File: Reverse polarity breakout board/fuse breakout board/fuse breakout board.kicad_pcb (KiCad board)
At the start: 2 copper layers, 8 parts

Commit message: yeo
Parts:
- moved Conn2 2.55 mm to (49.4, 44.1)
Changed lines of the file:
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@@
 	(footprint "MRDT_Connectors:Anderson_1_Horizontal"
 		(layer "F.Cu")
-		(at 49.8518 41.627)
+		(at 49.3518 44.127)
 		(property "Reference" "Conn2"
 			(at -5.588 4.572 0)

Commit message: We are almost finished
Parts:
- moved Conn2 83.3 mm to (61.1, 126.6)
- moved D1 81.0 mm to (85.3, 110.5)
- moved Conn1 56.5 mm to (61.1, 85.0)
- moved C4 47.9 mm to (97.6, 77.2)
- moved F1 47.7 mm to (87.4, 92.7), turned to -90 degrees
- moved C3 43.0 mm to (72.1, 68.5), turned to 90 degrees
- moved C1 37.9 mm to (89.9, 68.1), turned to 90 degrees
- moved C2 31.9 mm to (59.4, 70.6), turned to 180 degrees
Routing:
- added copper zone on F.Cu, net +BATT
- added copper zone on B.Cu, net GND
- added copper zone on F.Cu, net Net-(D1-K)
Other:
- board outline added: 69.6 x 82.8 mm
- board text added: "Reverse Polarity Fuse Board, Rev 1 Mars Rover Design Team Missouri S&T, 2024 Luke Duff, Sean Duda, Ethan Coggschell"

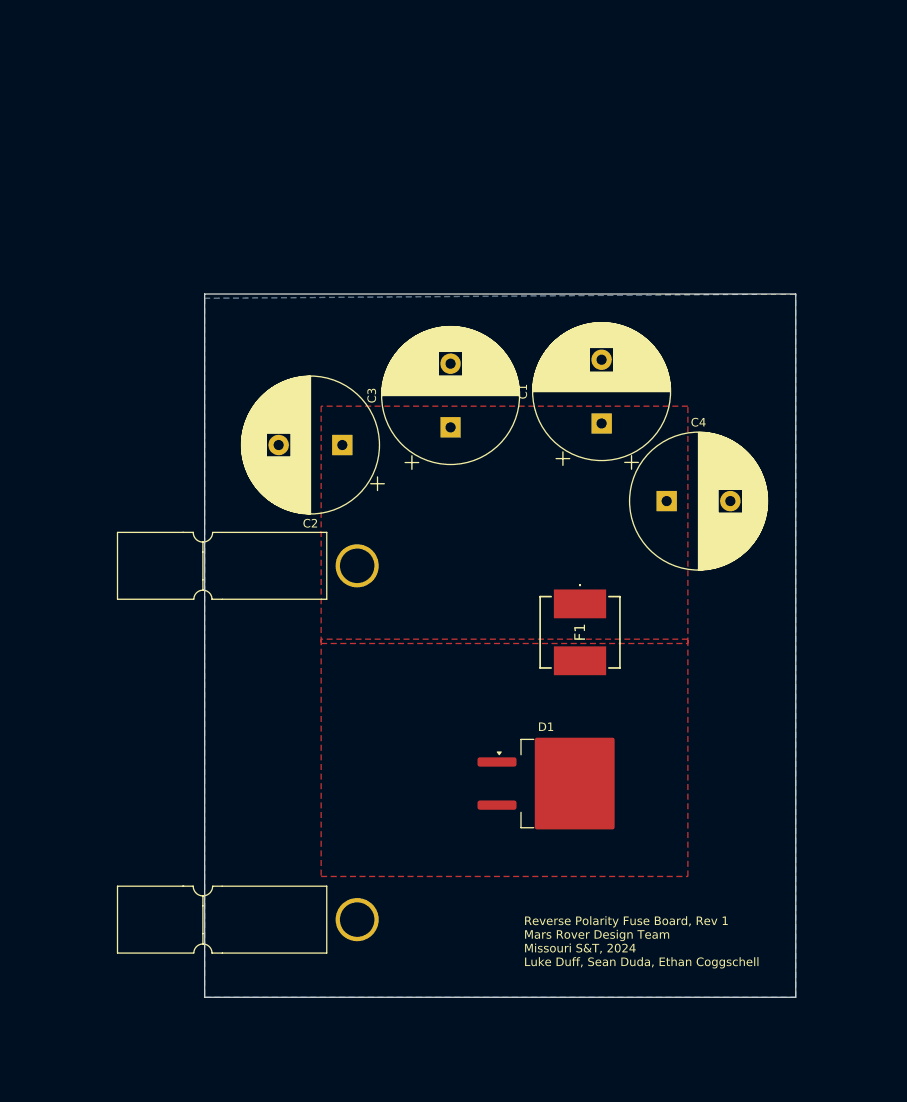
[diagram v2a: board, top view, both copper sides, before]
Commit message: Reworked power planes and adjusted cap bank
Reworked power plane and adjusted cap bank. Created a 35 mill trace from heatsink die to pad off power plane to account for ground connection
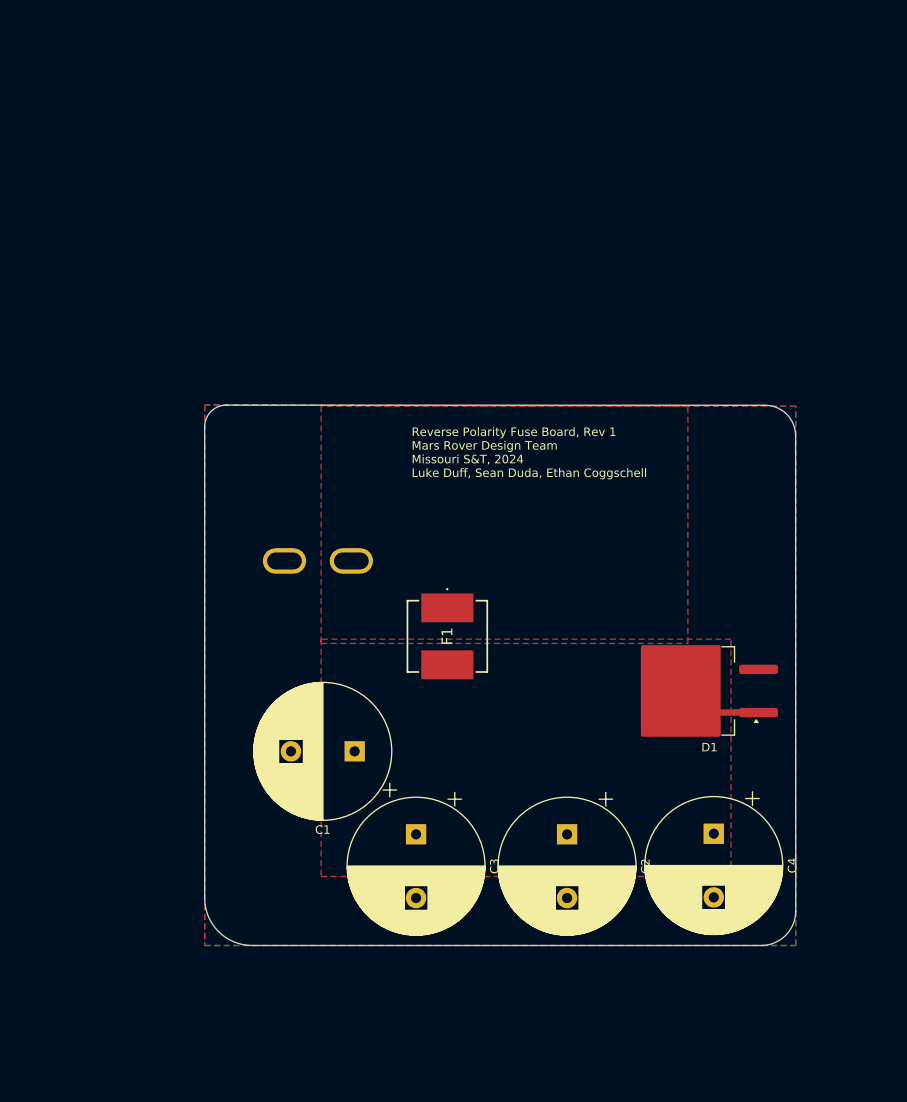
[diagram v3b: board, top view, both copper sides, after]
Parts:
- removed Conn2: AndersonPP, MRDT_Connectors:Anderson_1_Horizontal
- Conn1: footprint MRDT_Connectors:Anderson_1_Horizontal -> MRDT_Connectors:Square_Anderson_2_H_Side_By_Side_PV; moved to B.Cu
- moved C2 52.9 mm to (85.9, 116.5), turned to -90 degrees
- moved C1 48.3 mm to (60.8, 106.7), turned to 180 degrees
- moved C3 48.1 mm to (68.1, 116.5), turned to -90 degrees
- moved C4 39.5 mm to (103.1, 116.4), turned to -90 degrees
- moved D1 18.9 mm to (100.7, 99.6), turned to 180 degrees
- moved F1 15.6 mm to (71.8, 93.1)
- moved Conn1 8.85 mm to (52.3, 84.4), turned to -90 degrees
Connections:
- Conn1 pad 1: (no net) -> GND
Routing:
- net Net-(D1-K): track 0.00 -> 10.2 mm
- added copper zone on F.Cu, net GND
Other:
- board size 69.6 x 82.8 mm -> 69.6 x 63.6 mm

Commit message: Added Load Tester andersons and via stitching
Added load tester andersons and vias to stitch ground planes on the front and back together to prevent capacitance build up and allow current to flow
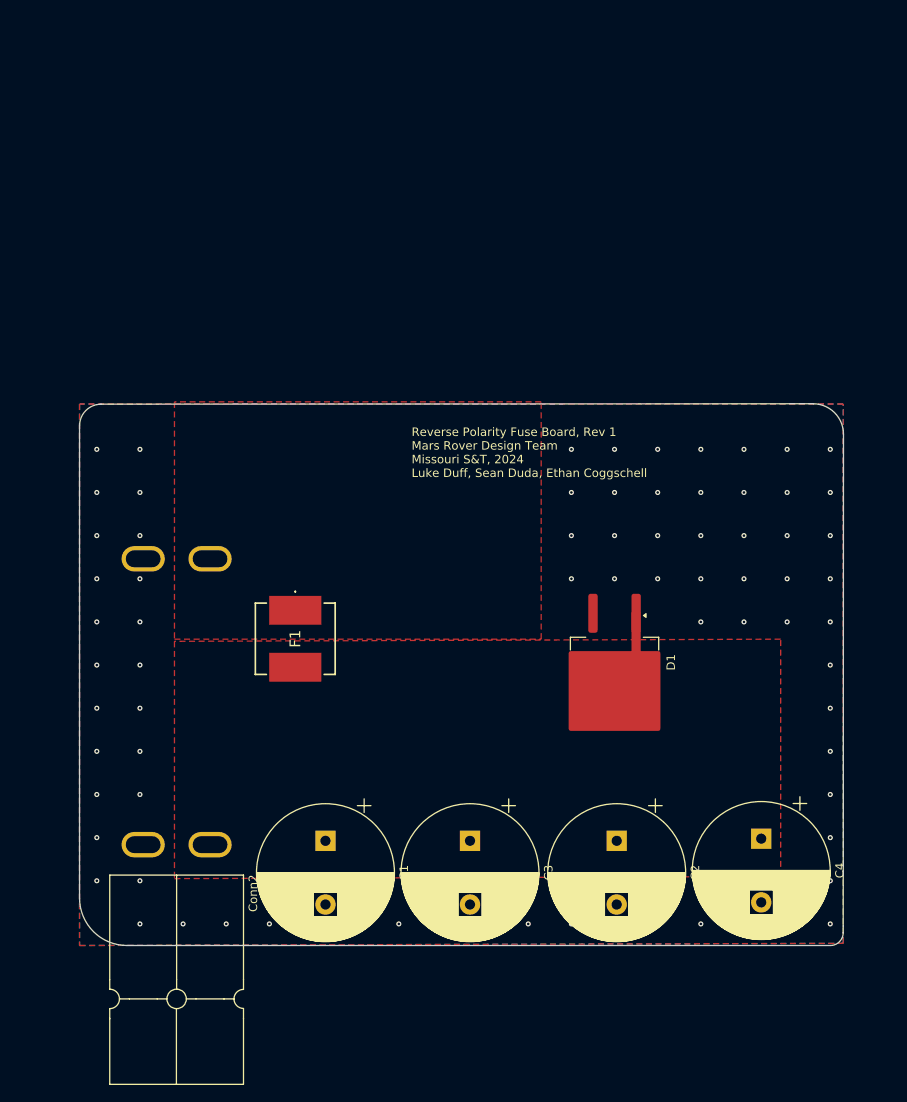
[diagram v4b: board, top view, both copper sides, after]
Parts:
- added Conn2: AndersonPP, MRDT_Connectors:Square_Anderson_2_H_Side_By_Side_PV, F.Cu at (35.6, 117.5)
- moved F1 17.9 mm to (53.8, 93.4)
- moved Conn1 16.6 mm to (35.6, 84.1)
- moved C1 11.1 mm to (57.4, 117.2), turned to -90 degrees
- moved D1 9.42 mm to (91.4, 98.1), turned to -90 degrees
- moved C3 6.40 mm to (74.4, 117.2)
- moved C2 5.89 mm to (91.7, 117.2)
- moved C4 5.62 mm to (108.7, 117.0)
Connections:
- net Net-(D1-K) renamed Load_Tester
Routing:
- net GND: vias 0 -> 76
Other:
- board size 69.6 x 63.6 mm -> 89.9 x 63.8 mm
